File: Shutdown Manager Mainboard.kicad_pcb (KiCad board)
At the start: 2 copper layers, 84.3 x 39.4 mm, 22 parts, among them J1 Conn_01x04, J2 Conn_01x03, J3 Conn_01x03, J6 Conn_01x03, K1 Relay_SPST_Panasonic_DJH-Form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, U1 Seeed Studio XIAO SAMD21, U2 TPS76133DBVR, U3 DRV8220DSGR, U4 DRV8220DSGR

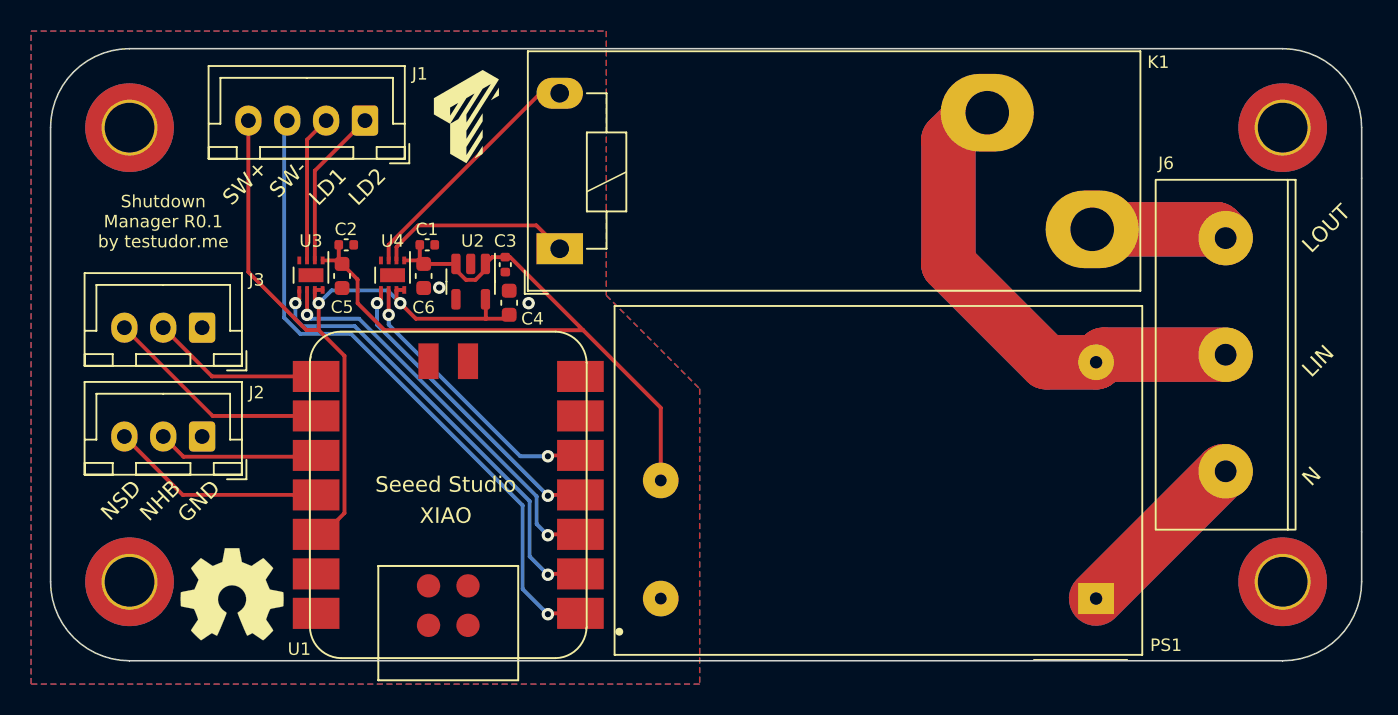
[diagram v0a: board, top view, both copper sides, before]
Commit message: Added strong external pullup/-down resistors to inputs, Added RC filter to main power button input
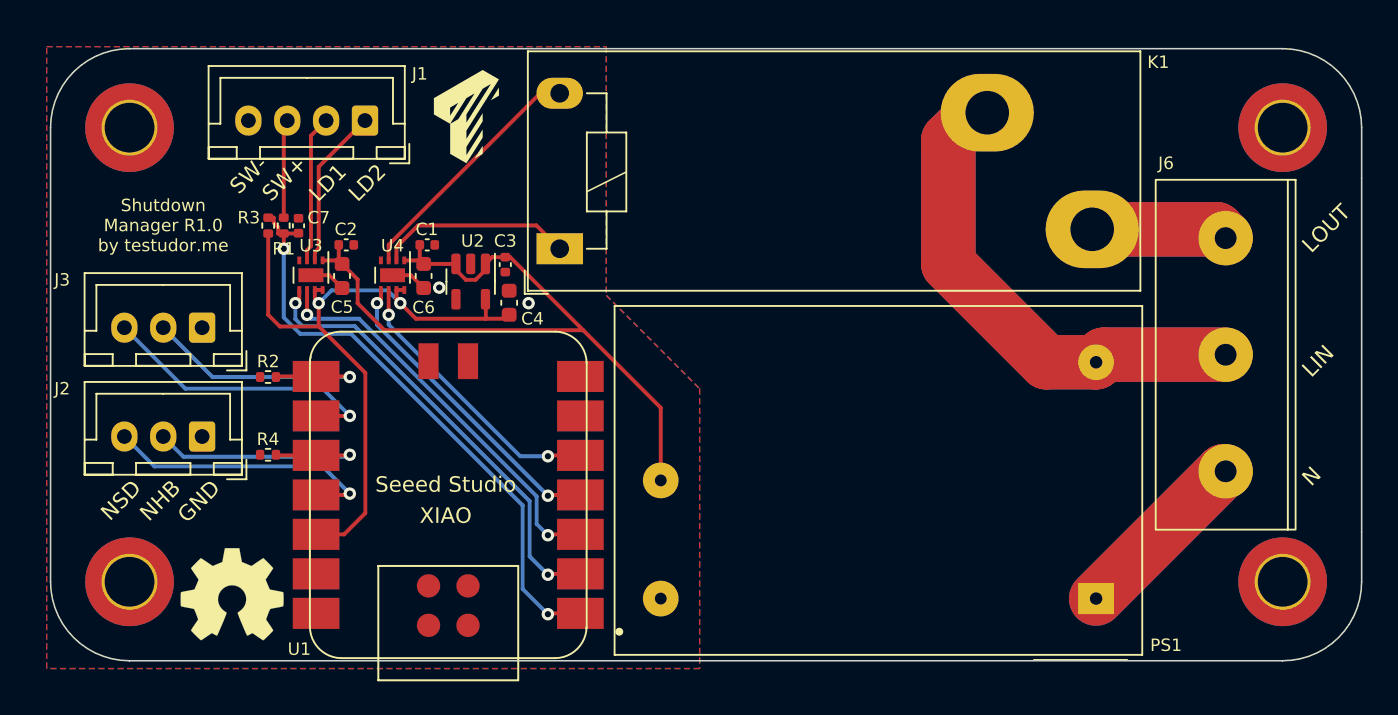
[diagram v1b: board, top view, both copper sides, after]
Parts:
- added C7: 1uF, Capacitor_SMD:C_0402_1005Metric, F.Cu at (126.2, 86.5)
- added R1: 10k, Resistor_SMD:R_0402_1005Metric, F.Cu at (125.2, 86.5)
- added R2: 1k, Resistor_SMD:R_0402_1005Metric, F.Cu at (124.2, 96.2)
- added R3: 1k, Resistor_SMD:R_0402_1005Metric, F.Cu at (124.2, 86.5)
- added R4: 1k, Resistor_SMD:R_0402_1005Metric, F.Cu at (124.2, 101.2)
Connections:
- J1 pad 3: POW_SW_1 -> Net-(J1-Pin_3)
- J1 pad 4: +3.3V -> GND
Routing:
- net NODE_HEARTBEAT_2: track 10.4 -> 17.4 mm, vias 0 -> 1
- net NODE_HEARTBEAT_1: track 11.1 -> 18.1 mm, vias 0 -> 1
- net Net-(J1-Pin_3): track 0.00 -> 6.34 mm
- net +3.3V: track 50.0 -> 44.9 mm
- net GND: track 0.00 -> 4.68 mm
- net POW_SW_1: track 42.9 -> 38.4 mm, vias 1 -> 2
- net NODE_SHUTDOWN_2: track 13.9 -> 18.2 mm, vias 0 -> 1
- net NODE_SHUTDOWN_1: track 14.7 -> 19.0 mm, vias 0 -> 1
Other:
- board text added: "PCB3D_BR_SD-MGR-MB"
- board text added: "PCB3D_TL_SD-MGR-MB"
- board text added: "Shutdown Manager R1.0 by testudor.me"
- board text removed: "Shutdown Manager R0.1 by testudor.me"

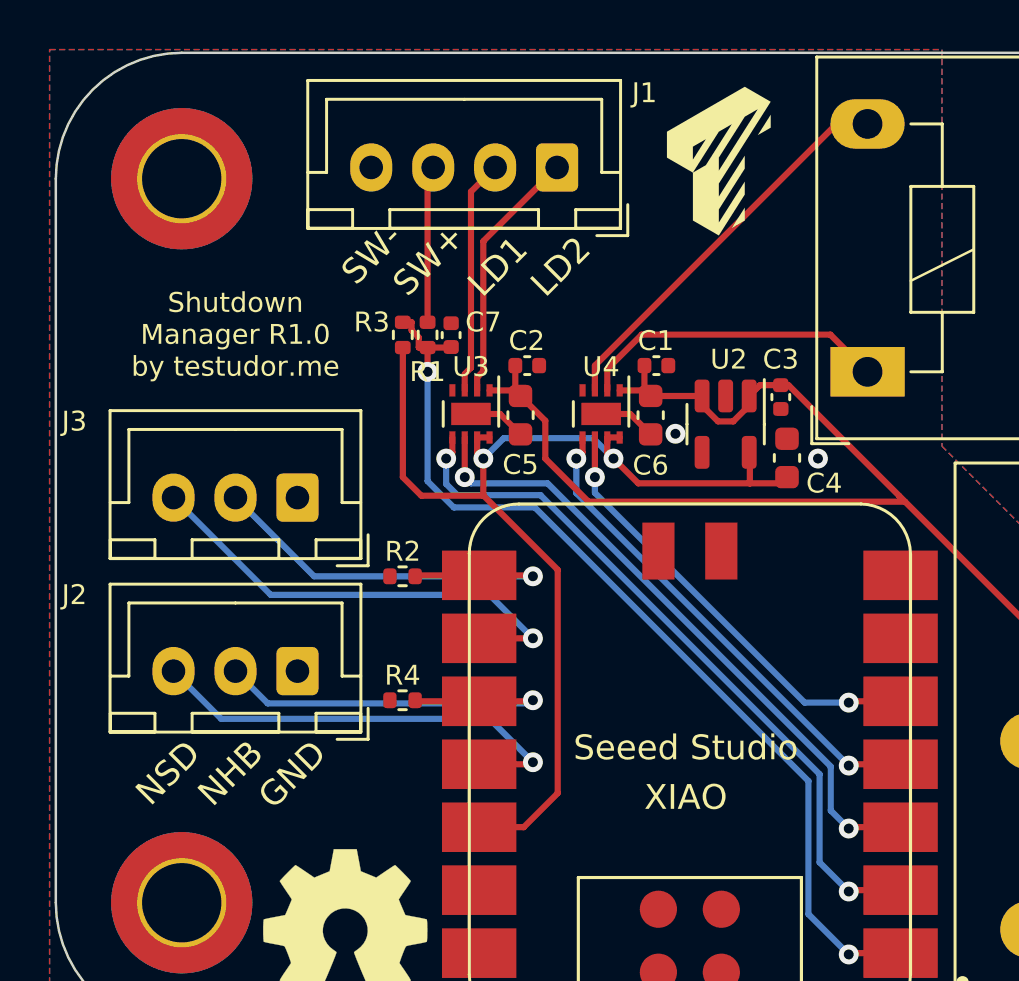
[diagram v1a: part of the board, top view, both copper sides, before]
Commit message: Fixed heartbeat input filtering
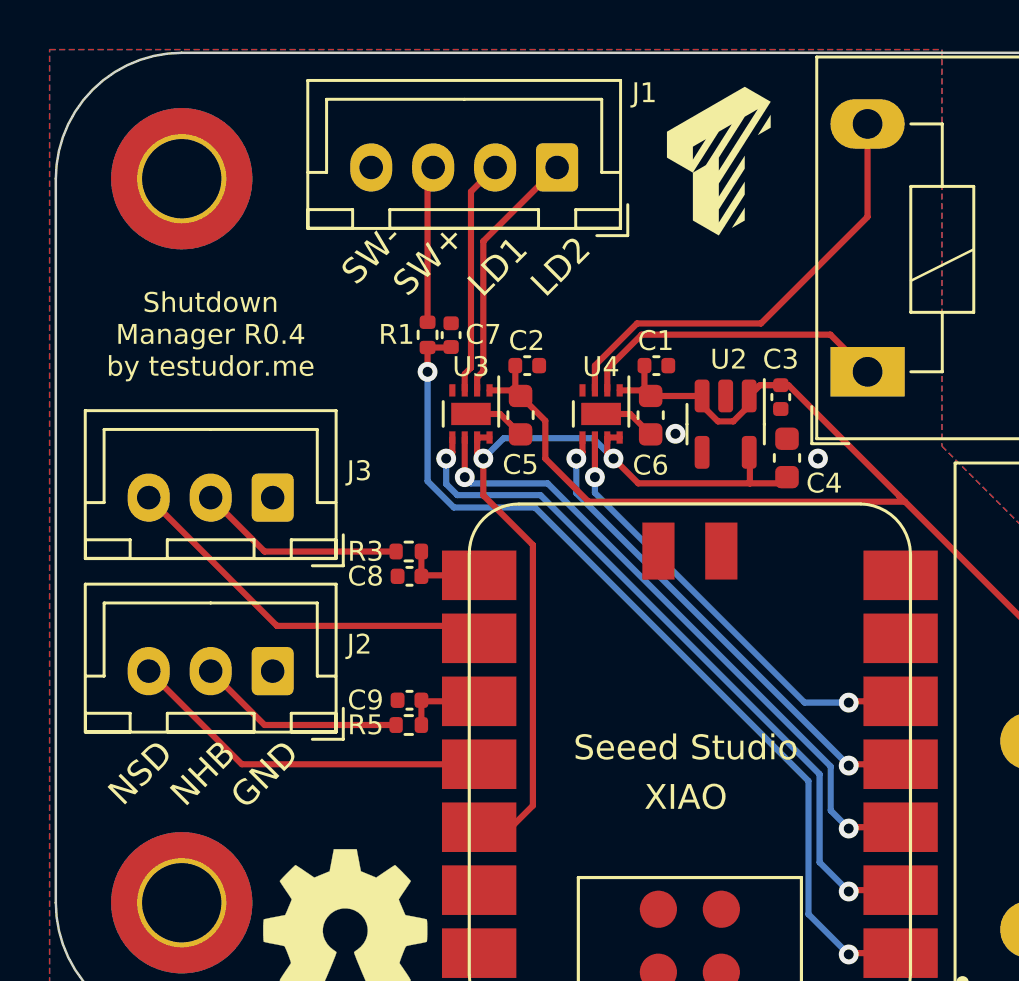
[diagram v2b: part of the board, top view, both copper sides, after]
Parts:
- removed R2, R4: 1k, Resistor_SMD:R_0402_1005Metric
- added C8: 0.1uF, Capacitor_SMD:C_0402_1005Metric, F.Cu at (124.5, 96.2)
- added C9: 0.1uF, Capacitor_SMD:C_0402_1005Metric, F.Cu at (124.5, 101.2)
- added R5: 10k, Resistor_SMD:R_0402_1005Metric, F.Cu at (124.5, 102.2)
- C7: value 1uF -> 0.1uF
- R3: value 1k -> 10k
- moved R3 8.74 mm to (124.5, 95.2), turned to 0 degrees
- moved J2 7.07 mm to (119.0, 93.1)
- moved J3 7.07 mm to (119.0, 100.1)
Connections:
- J2 pad 2: NODE_HEARTBEAT_2 -> Net-(J2-Pin_2)
- J2 pad 3: NODE_SHUTDOWN_2 -> NSD_1
- J3 pad 2: NODE_HEARTBEAT_1 -> Net-(J3-Pin_2)
- J3 pad 3: NODE_SHUTDOWN_1 -> NSD_2
- R3 pad 1: POW_SW_1 -> Net-(J2-Pin_2)
- R3 pad 2: +3.3V -> NHB_1
- U1 pad 10: NODE_HEARTBEAT_2 -> NHB_2
- U1 pad 11: NODE_SHUTDOWN_2 -> NSD_2
- U1 pad 8: NODE_HEARTBEAT_1 -> NHB_1
- U1 pad 9: NODE_SHUTDOWN_1 -> NSD_1
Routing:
- net NODE_SHUTDOWN_1: track 19.0 -> 0.00 mm, vias 1 -> 0
- net NODE_SHUTDOWN_2: track 18.2 -> 0.00 mm, vias 1 -> 0
- net NODE_HEARTBEAT_1: track 18.1 -> 0.00 mm, vias 1 -> 0
- net NODE_HEARTBEAT_2: track 17.4 -> 0.00 mm, vias 1 -> 0
- net NSD_1: track 0.00 -> 15.7 mm
- net NSD_2: track 0.00 -> 14.9 mm
- net +3.3V: track 44.9 -> 34.9 mm
- net Net-(J3-Pin_2): track 0.00 -> 8.38 mm
- net Net-(J2-Pin_2): track 0.00 -> 8.38 mm
- net NHB_1: track 0.00 -> 3.36 mm
- net NHB_2: track 0.00 -> 3.35 mm
- net RELAY_2: track 16.0 -> 18.2 mm
- net POW_SW_1: track 38.4 -> 36.5 mm
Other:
- board text added: "Shutdown Manager R0.4 by testudor.me"
- board text removed: "Shutdown Manager R1.0 by testudor.me"
